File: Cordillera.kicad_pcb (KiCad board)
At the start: 2 copper layers, 337.2 x 122.6 mm, 209 parts, among them J1 Conn_01x08, Q1 2N7002, Q2 2N7002, SW1 SW_SPST, U1 STM32F072CBTx, U2 XC6206P332MR, U3 SRV05-4

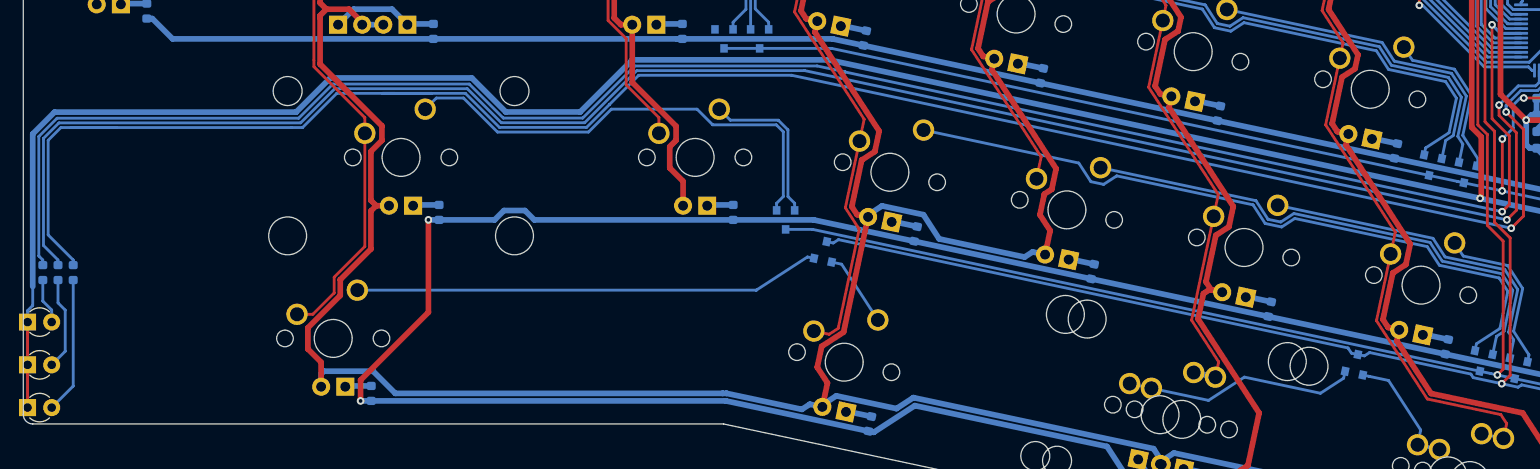
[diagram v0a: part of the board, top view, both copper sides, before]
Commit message: fix indicator leds
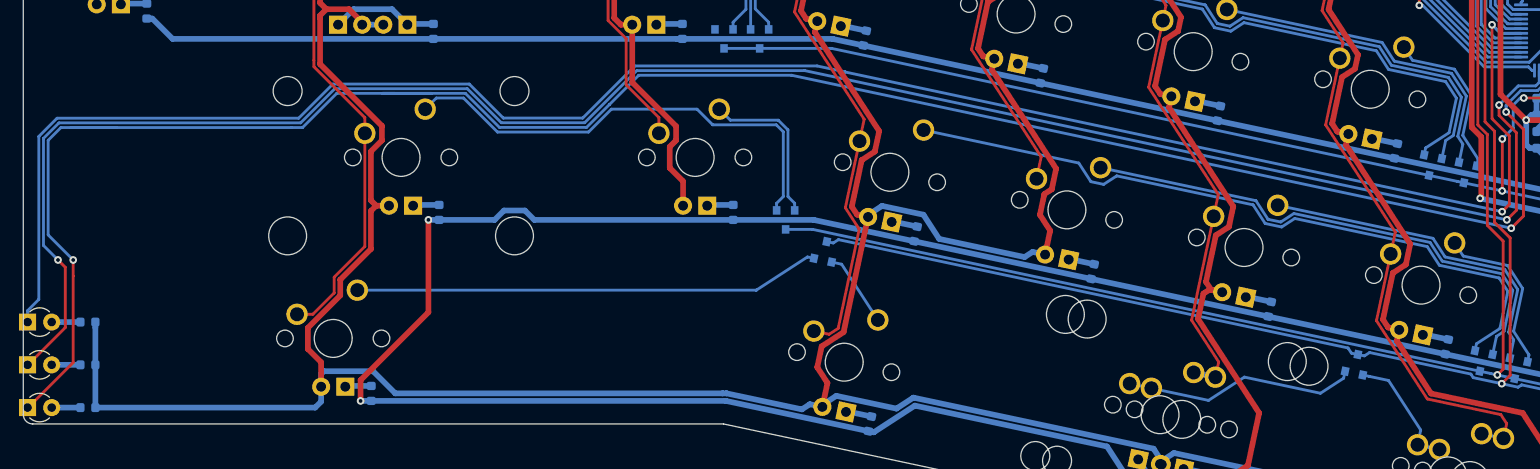
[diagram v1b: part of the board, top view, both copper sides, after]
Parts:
- moved R77 14.3 mm to (-2.20, 85.6), turned to 0 degrees
- moved R76 10.2 mm to (-2.20, 81.1), turned to 0 degrees
- moved R75 7.05 mm to (-2.20, 76.6), turned to 0 degrees
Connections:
- D38 pad 1: GND -> /B0
- D39 pad 1: GND -> /A1
- D40 pad 1: GND -> /A0
- R75 pad 2: /B0 -> +5V
- R76 pad 2: /A1 -> +5V
- R77 pad 2: /A0 -> +5V
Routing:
- net GND: track 401.0 -> 202.0 mm
- net +5V: track 1853.4 -> 1888.0 mm
- net /A0: track 207.5 -> 224.5 mm, vias 2 -> 3
- net /A1: track 195.3 -> 207.8 mm, vias 2 -> 3
- net Net-(D40-Pad2): track 14.4 -> 3.02 mm
- net Net-(D39-Pad2): track 9.83 -> 3.02 mm
- net /B0: track 202.4 -> 208.7 mm
- net Net-(D38-Pad2): track 4.81 -> 3.02 mm
